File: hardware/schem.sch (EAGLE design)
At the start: 6 parts, among them IC1 7805L, IC2 TLE5205-2, U2 TINY85-20-DIP

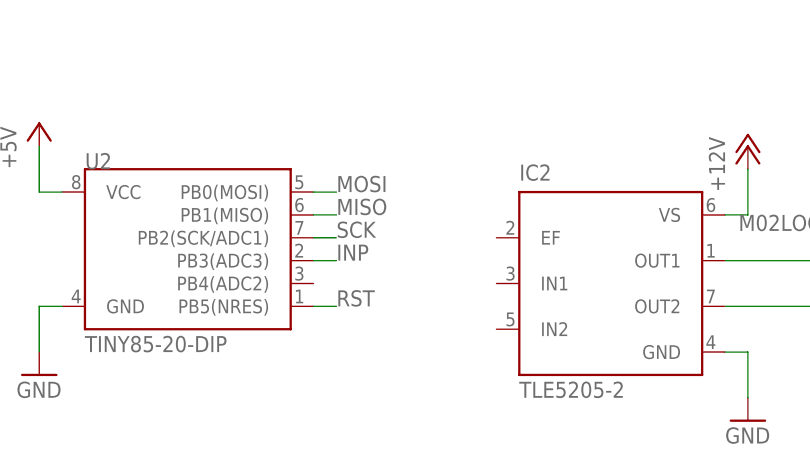
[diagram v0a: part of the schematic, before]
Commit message: added connections from tiny to HBridge
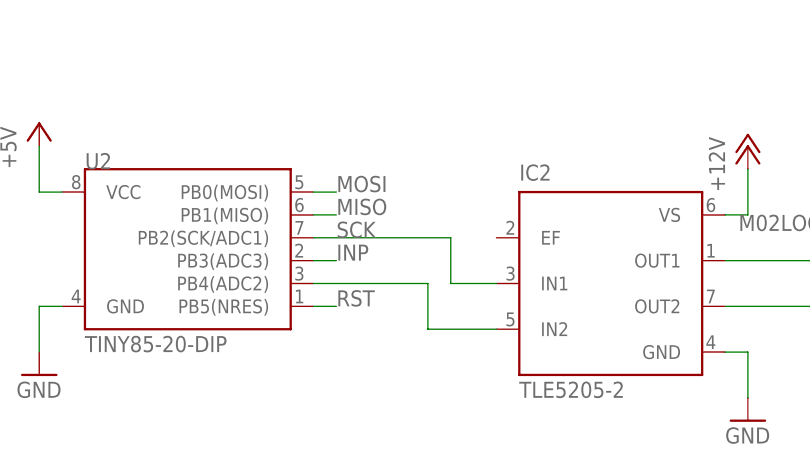
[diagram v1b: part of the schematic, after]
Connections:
- new net N$2: IC2.IN2, U2.PB4(ADC2)
- net SCK: now also IC2.IN1
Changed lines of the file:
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@@
 <segment>
 <pinref part="U2" gate="G$1" pin="PB2(SCK/ADC1)"/>
-<wire x1="86.36" y1="45.72" x2="88.9" y2="45.72" width="0.1524" layer="91"/>
 <label x="88.9" y="45.72" size="1.778" layer="95"/>
+<wire x1="86.36" y1="45.72" x2="101.6" y2="45.72" width="0.1524" layer="91"/>
+<wire x1="101.6" y1="45.72" x2="101.6" y2="40.64" width="0.1524" layer="91"/>
+<pinref part="IC2" gate="G$1" pin="IN1"/>
+<wire x1="101.6" y1="40.64" x2="106.68" y2="40.64" width="0.1524" layer="91"/>
 </segment>
 <segment>
@@
 </segment>
 </net>
+<net name="N$2" class="0">
+<segment>
+<pinref part="U2" gate="G$1" pin="PB4(ADC2)"/>
+<wire x1="86.36" y1="40.64" x2="99.06" y2="40.64" width="0.1524" layer="91"/>
+<wire x1="99.06" y1="40.64" x2="99.06" y2="35.56" width="0.1524" layer="91"/>
+<pinref part="IC2" gate="G$1" pin="IN2"/>
+<wire x1="99.06" y1="35.56" x2="106.68" y2="35.56" width="0.1524" layer="91"/>
+</segment>
+</net>

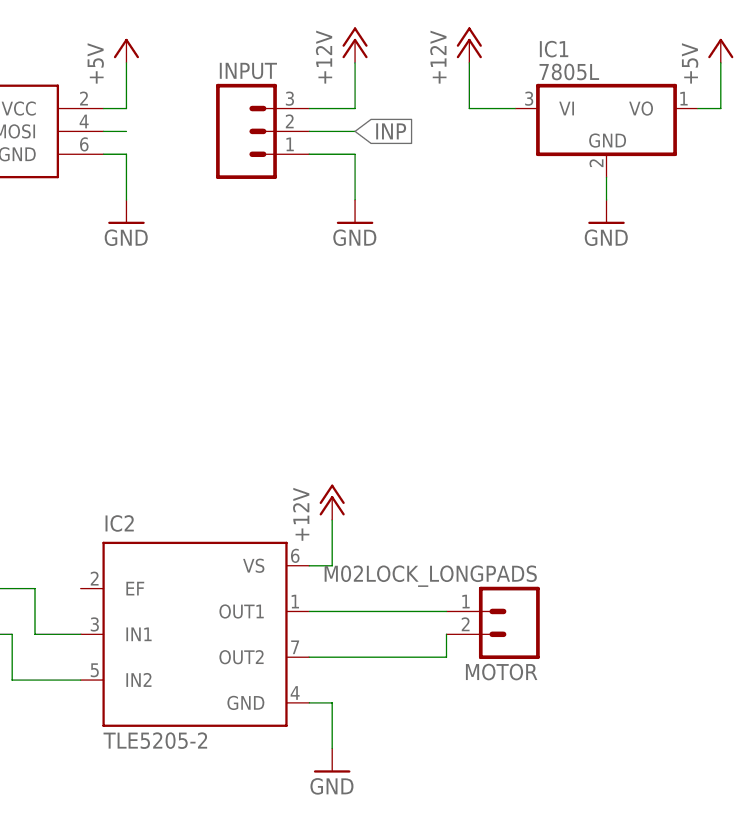
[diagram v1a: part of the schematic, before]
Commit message: changed pin inputs and re-rounted
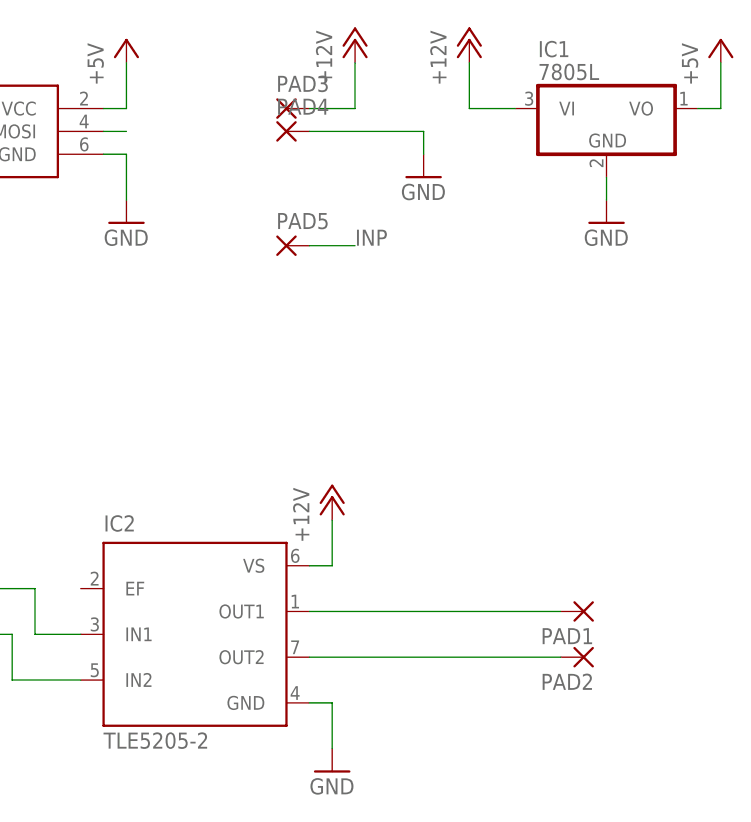
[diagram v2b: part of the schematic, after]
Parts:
- removed INPUT: (no value), SparkFun-Connectors:M03LOCK_LONGPADS
- removed MOTOR: M02LOCK_LONGPADS, SparkFun-Connectors:M02LOCK_LONGPADS
- added PAD1, PAD2, PAD3, PAD4: (no value), wirepad:3,81/1,4
- added PAD5: (no value), wirepad:1,6/0,9
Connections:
- net +12V: now also PAD3.P; no longer INPUT.3
- net GND: now also PAD4.P; no longer INPUT.1
- net INP: now also PAD5.P; no longer INPUT.2
- net N$1: now also PAD1.P; no longer MOTOR.1
- net N$4: now also PAD2.P; no longer MOTOR.2
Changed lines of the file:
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@@
 </classes>
 <parts>
-<part name="MOTOR" library="SparkFun-Connectors" deviceset="M02" device="LOCK_LONGPADS"/>
-<part name="INPUT" library="SparkFun-Connectors" deviceset="M03" device="LOCK_LONGPADS"/>
 <part name="IC1" library="linear" deviceset="78*" device="L" technology="05"/>
 <part name="IC2" library="infineon" deviceset="TLE5205-2" device=""/>
@@
 <part name="GND5" library="supply1" deviceset="GND" device=""/>
 <part name="P+6" library="supply1" deviceset="+5V" device=""/>
+<part name="PAD1" library="wirepad" deviceset="3,81/1,4" device=""/>
+<part name="PAD2" library="wirepad" deviceset="3,81/1,4" device=""/>
+<part name="PAD3" library="wirepad" deviceset="3,81/1,4" device=""/>
+<part name="PAD4" library="wirepad" deviceset="3,81/1,4" device=""/>
+<part name="PAD5" library="wirepad" deviceset="1,6/0,9" device=""/>
 </parts>
 <sheets>
@@
 </plain>
 <instances>
-<instance part="MOTOR" gate="G$1" x="154.94" y="43.18" rot="R180"/>
-<instance part="INPUT" gate="G$1" x="124.46" y="96.52"/>
 <instance part="IC1" gate="A1" x="165.1" y="99.06"/>
 <instance part="IC2" gate="G$1" x="119.38" y="40.64"/>
 <instance part="ISP1" gate="G$1" x="93.98" y="96.52"/>
 <instance part="P+1" gate="1" x="137.16" y="106.68"/>
-<instance part="GND1" gate="1" x="137.16" y="86.36"/>
+<instance part="GND1" gate="1" x="144.78" y="91.44"/>
 <instance part="P+2" gate="1" x="134.62" y="55.88"/>
 <instance part="P+3" gate="1" x="149.86" y="106.68"/>
@@
 <instance part="GND5" gate="1" x="55.88" y="30.48"/>
 <instance part="P+6" gate="1" x="55.88" y="58.42"/>
+<instance part="PAD1" gate="1" x="162.56" y="43.18" rot="R180"/>
+<instance part="PAD2" gate="1" x="162.56" y="38.1" rot="R180"/>
+<instance part="PAD3" gate="1" x="129.54" y="99.06"/>
+<instance part="PAD4" gate="1" x="129.54" y="96.52"/>
+<instance part="PAD5" gate="1" x="129.54" y="83.82"/>
 </instances>
 <busses>
@@
 <pinref part="P+1" gate="1" pin="+12V"/>
 <wire x1="137.16" y1="104.14" x2="137.16" y2="99.06" width="0.1524" layer="91"/>
-<pinref part="INPUT" gate="G$1" pin="3"/>
 <wire x1="137.16" y1="99.06" x2="132.08" y2="99.06" width="0.1524" layer="91"/>
+<pinref part="PAD3" gate="1" pin="P"/>
 </segment>
 <segment>
@@
 </net>
 <net name="GND" class="0">
-<segment>
-<pinref part="INPUT" gate="G$1" pin="1"/>
-<pinref part="GND1" gate="1" pin="GND"/>
-<wire x1="132.08" y1="93.98" x2="137.16" y2="93.98" width="0.1524" layer="91"/>
-<wire x1="137.16" y1="93.98" x2="137.16" y2="88.9" width="0.1524" layer="91"/>
-</segment>
 <segment>
 <pinref part="IC1" gate="A1" pin="GND"/>
@@
 <wire x1="55.88" y1="38.1" x2="55.88" y2="33.02" width="0.1524" layer="91"/>
 <pinref part="GND5" gate="1" pin="GND"/>
+</segment>
+<segment>
+<wire x1="132.08" y1="96.52" x2="144.78" y2="96.52" width="0.1524" layer="91"/>
+<pinref part="GND1" gate="1" pin="GND"/>
+<wire x1="144.78" y1="96.52" x2="144.78" y2="93.98" width="0.1524" layer="91"/>
+<pinref part="PAD4" gate="1" pin="P"/>
 </segment>
 </net>
@@
 <segment>
 <pinref part="IC2" gate="G$1" pin="OUT1"/>
-<pinref part="MOTOR" gate="G$1" pin="1"/>
-<wire x1="132.08" y1="43.18" x2="147.32" y2="43.18" width="0.1524" layer="91"/>
+<wire x1="132.08" y1="43.18" x2="160.02" y2="43.18" width="0.1524" layer="91"/>
+<pinref part="PAD1" gate="1" pin="P"/>
 </segment>
 </net>
@@
 <segment>
 <pinref part="IC2" gate="G$1" pin="OUT2"/>
-<pinref part="MOTOR" gate="G$1" pin="2"/>
-<wire x1="132.08" y1="38.1" x2="147.32" y2="38.1" width="0.1524" layer="91"/>
-<wire x1="147.32" y1="38.1" x2="147.32" y2="40.64" width="0.1524" layer="91"/>
+<wire x1="132.08" y1="38.1" x2="160.02" y2="38.1" width="0.1524" layer="91"/>
+<pinref part="PAD2" gate="1" pin="P"/>
 </segment>
 </net>
 <net name="INP" class="0">
-<segment>
-<pinref part="INPUT" gate="G$1" pin="2"/>
-<wire x1="132.08" y1="96.52" x2="137.16" y2="96.52" width="0.1524" layer="91"/>
-<label x="137.16" y="96.52" size="1.778" layer="95" xref="yes"/>
-</segment>
 <segment>
 <pinref part="U2" gate="G$1" pin="PB3(ADC3)"/>
@@
 <label x="88.9" y="43.18" size="1.778" layer="95"/>
 </segment>
+<segment>
+<wire x1="132.08" y1="83.82" x2="137.16" y2="83.82" width="0.1524" layer="91"/>
+<label x="137.16" y="83.82" size="1.778" layer="95"/>
+<pinref part="PAD5" gate="1" pin="P"/>
+</segment>
 </net>

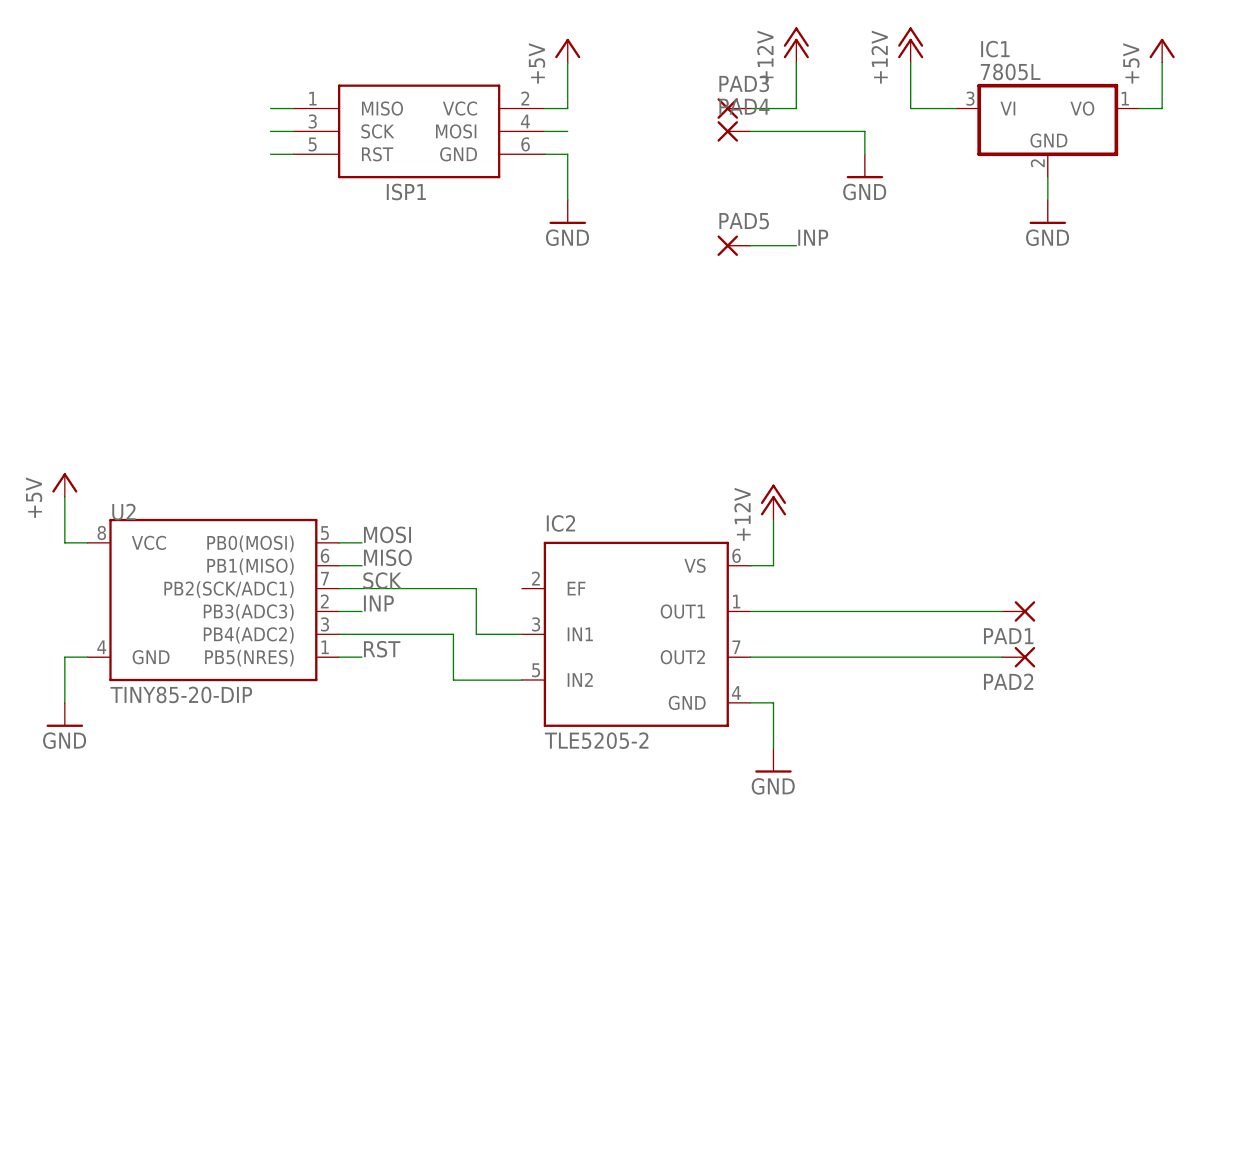
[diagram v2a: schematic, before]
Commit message: Updated Schematic
Used new IC H Bridge and cleaned up schematic
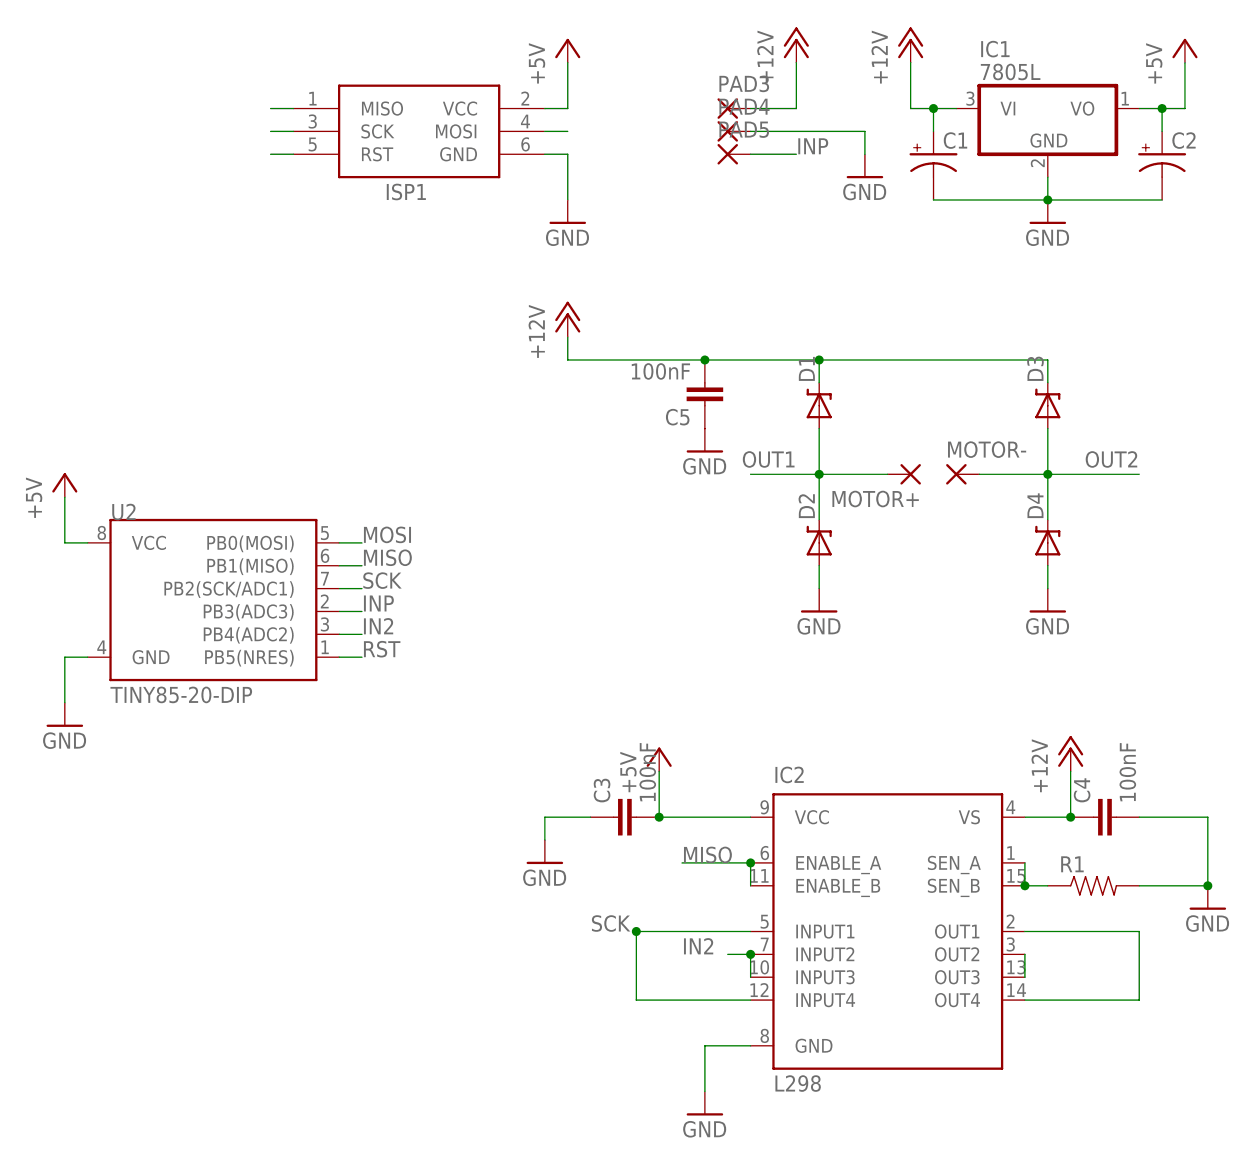
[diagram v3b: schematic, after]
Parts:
- removed PAD1, PAD2: (no value), wirepad:3,81/1,4
- added C1, C2: (no value), adafruit:CPOL-USE2.5-6
- added C3, C4, C5: 100nF, SparkFun-Capacitors:CAPPTH2
- added D1, D2, D3, D4: DIODE-ZENERPTH, SparkFun-DiscreteSemi:DIODE-ZENERPTH
- added MOTOR+, MOTOR-: (no value), wirepad:3,81/1,4
- added R1: (no value), SparkFun-Passives:RESISTORPTH-1/4W
- IC2: value TLE5205-2 -> L298; device infineon:TLE5205-2 -> st-microelectronics:L298
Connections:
- removed net N$2: IC2.IN2, U2.PB4(ADC2)
- removed net N$4: IC2.OUT2, PAD2.P
- new net IN2: IC2.INPUT2, IC2.INPUT3, U2.PB4(ADC2)
- new net OUT1: D1.A, D2.C, IC2.OUT1, IC2.OUT4, MOTOR+.P
- new net OUT2: D3.A, D4.C, IC2.OUT2, IC2.OUT3, MOTOR-.P
- net +12V: now also C1.+, C4.1, C5.2, D1.C, D3.C
- net +5V: now also C2.+, C3.2, IC2.VCC
- net GND: now also C1.-, C2.-, C3.1, C4.2, C5.1, D2.A, D4.A, R1.2
- net MISO: now also IC2.ENABLE_A, IC2.ENABLE_B
- net N$1: now also IC2.SEN_A, IC2.SEN_B, R1.1; no longer IC2.OUT1, PAD1.P
- net SCK: now also IC2.INPUT1, IC2.INPUT4; no longer IC2.IN1
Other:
- moved on the sheet: PAD5
